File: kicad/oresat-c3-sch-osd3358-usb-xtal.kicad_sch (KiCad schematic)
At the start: 43 parts, among them U1 OSD3358-512M-BSM, U11 RCLAMP0504FB, Y1 24MHz, Y2 Crystal

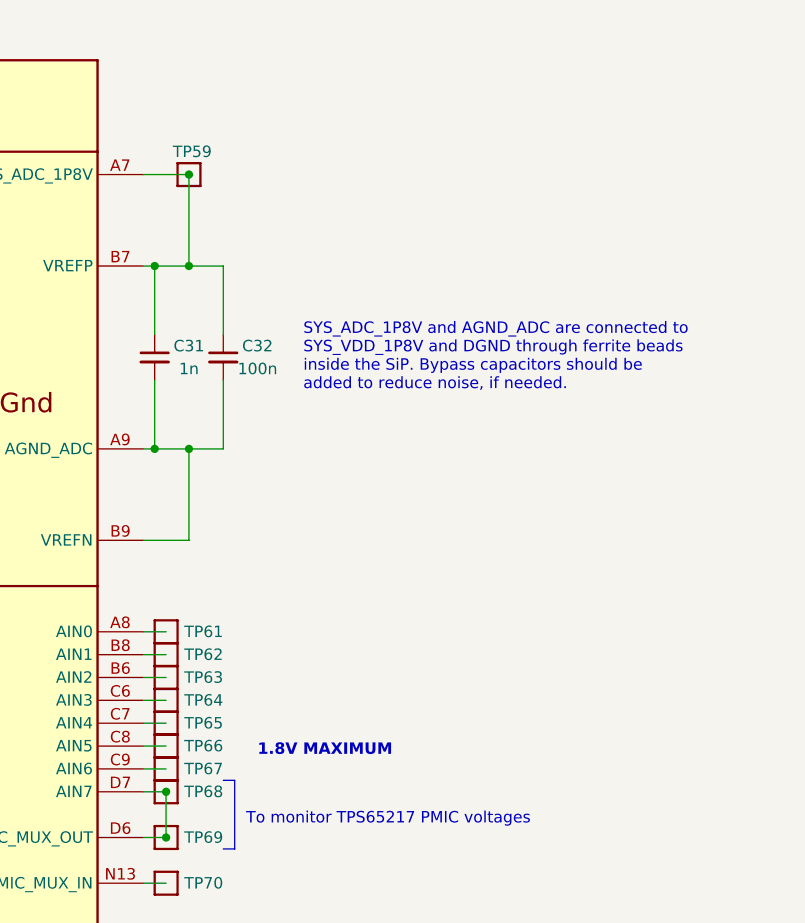
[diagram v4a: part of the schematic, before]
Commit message: Big C3 cleanup with Glenn; radios off of one SPS + separate LDOs, removed lots of test 0 ohm resistors, cleaned up capacitance, and finally wired everything up to the octavo. ZERO ERC errors.
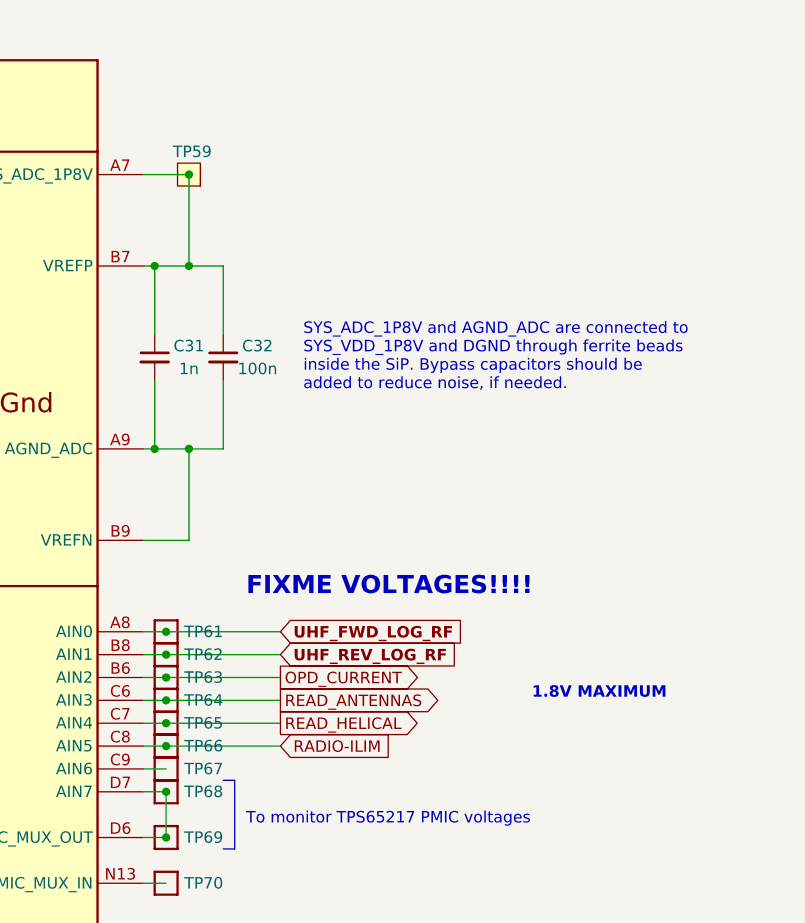
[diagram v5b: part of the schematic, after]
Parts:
- TP100, TP104, TP137, TP138, TP139, TP61, TP62, TP63, TP64, TP65, TP66, TP67, TP68, TP69, TP70, TP71, TP72, TP91, TP92, TP93, TP94, TP95, TP96, TP97, TP98, TP99: footprint oresat-misc:PAD.03X.04 -> TestPoint:TestPoint_Pad_D1.0mm; symbol oresat-misc:Test-Point -> oresat-misc:Test-Point-1mm-round
- TP59: footprint oresat-misc:PAD.03X.04 -> TestPoint:TestPoint_Pad_D1.0mm; symbol oresat-misc:Test-Point -> oresat-misc:Test-Point-0.75mm-th
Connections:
- net READ_HELICAL: now reaches TP65.1, U1.C7 (AIN4)
- net RADIO-ILIM: now reaches TP66.1, U1.C8 (AIN5)
- net UHF_FWD_LOG_RF: now reaches TP61.1, U1.A8 (AIN0)
- net OPD_CURRENT: now reaches TP63.1, U1.B6 (AIN2)
- net UHF_REV_LOG_RF: now reaches TP62.1, U1.B8 (AIN1)
- net READ_ANTENNAS: now reaches TP64.1, U1.C6 (AIN3)
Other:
- note added: "FIXME VOLTAGES!!!!"

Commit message: Fixed test points; added RF test points. Started on layout and component packages for UHF radio.
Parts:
- TP100, TP104, TP137, TP138, TP139, TP61, TP62, TP63, TP64, TP65, TP66, TP67, TP68, TP69, TP70, TP71, TP72, TP91, TP92, TP93, TP94, TP95, TP96, TP97, TP98, TP99: footprint TestPoint:TestPoint_Pad_D1.0mm -> oresat-misc:TestPoint_Pad_D1.0mm
- TP59: footprint TestPoint:TestPoint_Pad_D1.0mm -> oresat-misc:TestPoint-0.75mm-th
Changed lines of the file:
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@@
       (effects (font (size 1.27 1.27)) hide)
     )
-    (property "Footprint" "TestPoint:TestPoint_Pad_D1.0mm" (at 259.08 142.24 0)
+    (property "Footprint" "oresat-misc:TestPoint_Pad_D1.0mm" (at 259.08 142.24 0)
       (effects (font (size 1.27 1.27)) hide)
     )
@@
       (effects (font (size 1.27 1.27)) hide)
     )
-    (property "Footprint" "TestPoint:TestPoint_Pad_D1.0mm" (at 259.08 160.02 0)
+    (property "Footprint" "oresat-misc:TestPoint_Pad_D1.0mm" (at 259.08 160.02 0)
       (effects (font (size 1.27 1.27)) hide)
     )
@@
       (effects (font (size 1.27 1.27)) hide)
     )
-    (property "Footprint" "TestPoint:TestPoint_Pad_D1.0mm" (at 193.04 152.4 0)
+    (property "Footprint" "oresat-misc:TestPoint_Pad_D1.0mm" (at 193.04 152.4 0)
       (effects (font (size 1.27 1.27)) hide)
     )
@@
       (effects (font (size 1.27 1.27)) hide)
     )
-    (property "Footprint" "TestPoint:TestPoint_Pad_D1.0mm" (at 193.04 144.78 0)
+    (property "Footprint" "oresat-misc:TestPoint_Pad_D1.0mm" (at 193.04 144.78 0)
       (effects (font (size 1.27 1.27)) hide)
     )
@@
       (effects (font (size 1.27 1.27)) hide)
     )
-    (property "Footprint" "TestPoint:TestPoint_Pad_D1.0mm" (at 193.04 147.32 0)
+    (property "Footprint" "oresat-misc:TestPoint_Pad_D1.0mm" (at 193.04 147.32 0)
       (effects (font (size 1.27 1.27)) hide)
     )
@@
       (effects (font (size 1.27 1.27)) hide)
     )
-    (property "Footprint" "TestPoint:TestPoint_Pad_D1.0mm" (at 259.08 182.88 0)
+    (property "Footprint" "oresat-misc:TestPoint_Pad_D1.0mm" (at 259.08 182.88 0)
       (effects (font (size 1.27 1.27)) hide)
     )
@@
       (effects (font (size 1.27 1.27)) hide)
     )
-    (property "Footprint" "TestPoint:TestPoint_Pad_D1.0mm" (at 259.08 175.26 0)
+    (property "Footprint" "oresat-misc:TestPoint_Pad_D1.0mm" (at 259.08 175.26 0)
       (effects (font (size 1.27 1.27)) hide)
     )
@@
       (effects (font (size 1.27 1.27)) hide)
     )
-    (property "Footprint" "TestPoint:TestPoint_Pad_D1.0mm" (at 193.04 160.02 0)
+    (property "Footprint" "oresat-misc:TestPoint_Pad_D1.0mm" (at 193.04 160.02 0)
       (effects (font (size 1.27 1.27)) hide)
     )
@@
       (effects (font (size 1.27 1.27)) hide)
     )
-    (property "Footprint" "TestPoint:TestPoint_Pad_D1.0mm" (at 193.04 154.94 0)
+    (property "Footprint" "oresat-misc:TestPoint_Pad_D1.0mm" (at 193.04 154.94 0)
       (effects (font (size 1.27 1.27)) hide)
     )
@@
       (effects (font (size 1.27 1.27)) hide)
     )
-    (property "Footprint" "TestPoint:TestPoint_Pad_D1.0mm" (at 259.08 144.78 0)
+    (property "Footprint" "oresat-misc:TestPoint_Pad_D1.0mm" (at 259.08 144.78 0)
       (effects (font (size 1.27 1.27)) hide)
     )
@@
       (effects (font (size 1.27 1.27)) hide)
     )
-    (property "Footprint" "TestPoint:TestPoint_Pad_D1.0mm" (at 259.08 170.18 0)
+    (property "Footprint" "oresat-misc:TestPoint_Pad_D1.0mm" (at 259.08 170.18 0)
       (effects (font (size 1.27 1.27)) hide)
     )
@@
       (effects (font (size 1.27 1.27)) hide)
     )
-    (property "Footprint" "TestPoint:TestPoint_Pad_D1.0mm" (at 193.04 177.8 0)
+    (property "Footprint" "oresat-misc:TestPoint_Pad_D1.0mm" (at 193.04 177.8 0)
       (effects (font (size 1.27 1.27)) hide)
     )
@@
       (effects (font (size 1.27 1.27)) hide)
     )
-    (property "Footprint" "TestPoint:TestPoint_Pad_D1.0mm" (at 259.08 132.08 0)
+    (property "Footprint" "oresat-misc:TestPoint_Pad_D1.0mm" (at 259.08 132.08 0)
       (effects (font (size 1.27 1.27)) hide)
     )
@@
       (effects (font (size 1.27 1.27)) hide)
     )
-    (property "Footprint" "TestPoint:TestPoint_Pad_D1.0mm" (at 259.08 154.94 0)
+    (property "Footprint" "oresat-misc:TestPoint_Pad_D1.0mm" (at 259.08 154.94 0)
       (effects (font (size 1.27 1.27)) hide)
     )
@@
       (effects (font (size 1.27 1.27)) hide)
     )
-    (property "Footprint" "TestPoint:TestPoint_Pad_D1.0mm" (at 193.04 180.34 0)
+    (property "Footprint" "oresat-misc:TestPoint_Pad_D1.0mm" (at 193.04 180.34 0)
       (effects (font (size 1.27 1.27)) hide)
     )
@@
       (effects (font (size 1.27 1.27)) hide)
     )
-    (property "Footprint" "TestPoint:TestPoint_Pad_D1.0mm" (at 259.08 172.72 0)
+    (property "Footprint" "oresat-misc:TestPoint_Pad_D1.0mm" (at 259.08 172.72 0)
       (effects (font (size 1.27 1.27)) hide)
     )
@@
       (effects (font (size 1.27 1.27)) hide)
     )
-    (property "Footprint" "TestPoint:TestPoint_Pad_D1.0mm" (at 259.08 137.16 0)
+    (property "Footprint" "oresat-misc:TestPoint_Pad_D1.0mm" (at 259.08 137.16 0)
       (effects (font (size 1.27 1.27)) hide)
     )
@@
       (effects (font (size 1.27 1.27)) hide)
     )
-    (property "Footprint" "TestPoint:TestPoint_Pad_D1.0mm" (at 259.08 134.62 0)
+    (property "Footprint" "oresat-misc:TestPoint_Pad_D1.0mm" (at 259.08 134.62 0)
       (effects (font (size 1.27 1.27)) hide)
     )
@@
       (effects (font (size 1.27 1.27)) hide)
     )
-    (property "Footprint" "TestPoint:TestPoint_Pad_D1.0mm" (at 193.04 157.48 0)
+    (property "Footprint" "oresat-misc:TestPoint_Pad_D1.0mm" (at 193.04 157.48 0)
       (effects (font (size 1.27 1.27)) hide)
     )
@@
       (effects (font (size 1.27 1.27)) hide)
     )
-    (property "Footprint" "TestPoint:TestPoint_Pad_D1.0mm" (at 193.04 149.86 0)
+    (property "Footprint" "oresat-misc:TestPoint_Pad_D1.0mm" (at 193.04 149.86 0)
       (effects (font (size 1.27 1.27)) hide)
     )
@@
       (effects (font (size 1.27 1.27)) hide)
     )
-    (property "Footprint" "TestPoint:TestPoint_Pad_D1.0mm" (at 259.08 139.7 0)
+    (property "Footprint" "oresat-misc:TestPoint_Pad_D1.0mm" (at 259.08 139.7 0)
       (effects (font (size 1.27 1.27)) hide)
     )
@@
       (effects (font (size 1.27 1.27)) hide)
     )
-    (property "Footprint" "TestPoint:TestPoint_Pad_D1.0mm" (at 259.08 177.8 0)
+    (property "Footprint" "oresat-misc:TestPoint_Pad_D1.0mm" (at 259.08 177.8 0)
       (effects (font (size 1.27 1.27)) hide)
     )
@@
       (effects (font (size 1.27 1.27)) hide)
     )
-    (property "Footprint" "TestPoint:TestPoint_Pad_D1.0mm" (at 261.62 81.28 0)
+    (property "Footprint" "oresat-misc:TestPoint-0.75mm-th" (at 261.62 81.28 0)
       (effects (font (size 1.27 1.27)) hide)
     )
@@
       (effects (font (size 1.27 1.27)) hide)
     )
-    (property "Footprint" "TestPoint:TestPoint_Pad_D1.0mm" (at 259.08 149.86 0)
+    (property "Footprint" "oresat-misc:TestPoint_Pad_D1.0mm" (at 259.08 149.86 0)
       (effects (font (size 1.27 1.27)) hide)
     )
@@
       (effects (font (size 1.27 1.27)) hide)
     )
-    (property "Footprint" "TestPoint:TestPoint_Pad_D1.0mm" (at 259.08 180.34 0)
+    (property "Footprint" "oresat-misc:TestPoint_Pad_D1.0mm" (at 259.08 180.34 0)
       (effects (font (size 1.27 1.27)) hide)
     )
@@
       (effects (font (size 1.27 1.27)) hide)
     )
-    (property "Footprint" "TestPoint:TestPoint_Pad_D1.0mm" (at 259.08 147.32 0)
+    (property "Footprint" "oresat-misc:TestPoint_Pad_D1.0mm" (at 259.08 147.32 0)
       (effects (font (size 1.27 1.27)) hide)
     )
@@
       (effects (font (size 1.27 1.27)) hide)
     )
-    (property "Footprint" "TestPoint:TestPoint_Pad_D1.0mm" (at 193.04 182.88 0)
-      (effects (font (size 1.27 1.27)) hide)
-    )
+    (property "Footprint" "oresat-misc:TestPoint_Pad_D1.0mm" (at 193.04 182.88 0)
+      (effects (font (size 1.27 1.27)) hide)
+    )
